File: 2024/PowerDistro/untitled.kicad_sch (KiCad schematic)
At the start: 40 parts

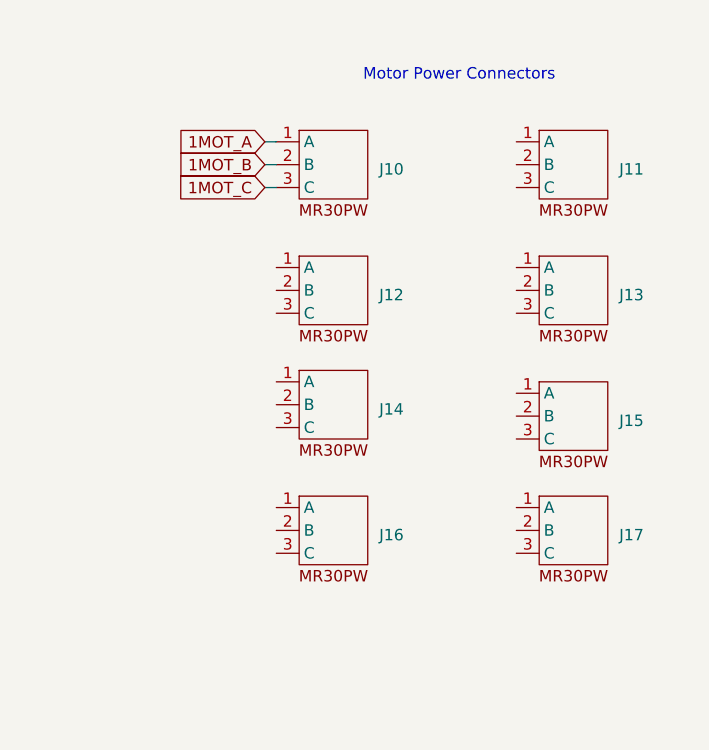
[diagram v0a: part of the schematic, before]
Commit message: changed motor controler numbers and hole numbers in PCB
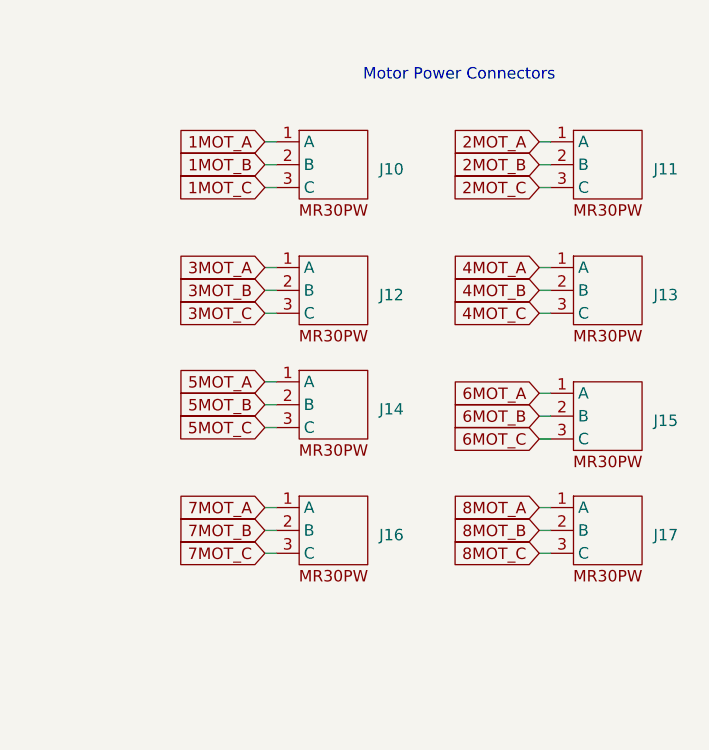
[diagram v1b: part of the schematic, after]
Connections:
- net 4MOT_A: now reaches J13.1 (A)
- net 4MOT_B: now reaches J13.2 (B)
- net 4MOT_C: now reaches J13.3 (C)
- net 7MOT_A: now reaches J16.1 (A)
- net 7MOT_B: now reaches J16.2 (B)
- net 7MOT_C: now reaches J16.3 (C)
- net 5MOT_A: now reaches J14.1 (A)
- net 5MOT_B: now reaches J14.2 (B)
- net 5MOT_C: now reaches J14.3 (C)
- net 6MOT_A: now reaches J15.1 (A)
- net 6MOT_B: now reaches J15.2 (B)
- net 6MOT_C: now reaches J15.3 (C)
- net 3MOT_A: now reaches J12.1 (A)
- net 3MOT_B: now reaches J12.2 (B)
- net 3MOT_C: now reaches J12.3 (C)
- net 2MOT_A: now reaches J11.1 (A)
- net 2MOT_B: now reaches J11.2 (B)
- net 2MOT_C: now reaches J11.3 (C)
- net 8MOT_A: now reaches J17.1 (A)
- net 8MOT_B: now reaches J17.2 (B)
- net 8MOT_C: now reaches J17.3 (C)
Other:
- moved on the sheet: J11, J13, J15, J17

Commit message: rearranged the power distro board
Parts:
- H1, H10, H11, H12, H13, H14, H15, H16, H17, H18, H19, H2, H20, H21, H22, H23, H24, H25, H26, H27, H28, H29, H3, H30, H31, H32, H4, H5, H6, H7, H8, H9: footprint (none) -> MountingHole:MountingHole_2.7mm_M2.5_ISO7380
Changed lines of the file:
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@@
 			)
 		)
-		(property "Footprint" ""
+		(property "Footprint" "MountingHole:MountingHole_2.7mm_M2.5_ISO7380"
 			(at 101.6 127 0)
 			(effects
@@
 			)
 		)
-		(property "Footprint" ""
+		(property "Footprint" "MountingHole:MountingHole_2.7mm_M2.5_ISO7380"
 			(at 101.6 81.28 0)
 			(effects
@@
 			)
 		)
-		(property "Footprint" ""
+		(property "Footprint" "MountingHole:MountingHole_2.7mm_M2.5_ISO7380"
 			(at 81.28 50.8 0)
 			(effects
@@
 			)
 		)
-		(property "Footprint" ""
+		(property "Footprint" "MountingHole:MountingHole_2.7mm_M2.5_ISO7380"
 			(at 101.6 119.38 0)
 			(effects
@@
 			)
 		)
-		(property "Footprint" ""
+		(property "Footprint" "MountingHole:MountingHole_2.7mm_M2.5_ISO7380"
 			(at 81.28 165.1 0)
 			(effects
@@
 			)
 		)
-		(property "Footprint" ""
+		(property "Footprint" "MountingHole:MountingHole_2.7mm_M2.5_ISO7380"
 			(at 81.28 127 0)
 			(effects
@@
 			)
 		)
-		(property "Footprint" ""
+		(property "Footprint" "MountingHole:MountingHole_2.7mm_M2.5_ISO7380"
 			(at 101.6 149.86 0)
 			(effects
@@
 			)
 		)
-		(property "Footprint" ""
+		(property "Footprint" "MountingHole:MountingHole_2.7mm_M2.5_ISO7380"
 			(at 101.6 88.9 0)
 			(effects
@@
 			)
 		)
-		(property "Footprint" ""
+		(property "Footprint" "MountingHole:MountingHole_2.7mm_M2.5_ISO7380"
 			(at 101.6 50.8 0)
 			(effects
@@
 			)
 		)
-		(property "Footprint" ""
+		(property "Footprint" "MountingHole:MountingHole_2.7mm_M2.5_ISO7380"
 			(at 101.6 66.04 0)
 			(effects
@@
 			)
 		)
-		(property "Footprint" ""
+		(property "Footprint" "MountingHole:MountingHole_2.7mm_M2.5_ISO7380"
 			(at 81.28 134.62 0)
 			(effects
@@
 			)
 		)
-		(property "Footprint" ""
+		(property "Footprint" "MountingHole:MountingHole_2.7mm_M2.5_ISO7380"
 			(at 101.6 142.24 0)
 			(effects
@@
 			)
 		)
-		(property "Footprint" ""
+		(property "Footprint" "MountingHole:MountingHole_2.7mm_M2.5_ISO7380"
 			(at 101.6 111.76 0)
 			(effects
@@
 			)
 		)
-		(property "Footprint" ""
+		(property "Footprint" "MountingHole:MountingHole_2.7mm_M2.5_ISO7380"
 			(at 101.6 165.1 0)
 			(effects
@@
 			)
 		)
-		(property "Footprint" ""
+		(property "Footprint" "MountingHole:MountingHole_2.7mm_M2.5_ISO7380"
 			(at 81.28 66.04 0)
 			(effects
@@
 			)
 		)
-		(property "Footprint" ""
+		(property "Footprint" "MountingHole:MountingHole_2.7mm_M2.5_ISO7380"
 			(at 101.6 73.66 0)
 			(effects
@@
 			)
 		)
-		(property "Footprint" ""
+		(property "Footprint" "MountingHole:MountingHole_2.7mm_M2.5_ISO7380"
 			(at 101.6 96.52 0)
 			(effects
@@
 			)
 		)
-		(property "Footprint" ""
+		(property "Footprint" "MountingHole:MountingHole_2.7mm_M2.5_ISO7380"
 			(at 81.28 81.28 0)
 			(effects
@@
 			)
 		)
-		(property "Footprint" ""
+		(property "Footprint" "MountingHole:MountingHole_2.7mm_M2.5_ISO7380"
 			(at 81.28 157.48 0)
 			(effects
@@
 			)
 		)
-		(property "Footprint" ""
+		(property "Footprint" "MountingHole:MountingHole_2.7mm_M2.5_ISO7380"
 			(at 101.6 104.14 0)
 			(effects
@@
 			)
 		)
-		(property "Footprint" ""
+		(property "Footprint" "MountingHole:MountingHole_2.7mm_M2.5_ISO7380"
 			(at 81.28 149.86 0)
 			(effects
@@
 			)
 		)
-		(property "Footprint" ""
+		(property "Footprint" "MountingHole:MountingHole_2.7mm_M2.5_ISO7380"
 			(at 81.28 104.14 0)
 			(effects
@@
 			)
 		)
-		(property "Footprint" ""
+		(property "Footprint" "MountingHole:MountingHole_2.7mm_M2.5_ISO7380"
 			(at 81.28 119.38 0)
 			(effects
@@
 			)
 		)
-		(property "Footprint" ""
+		(property "Footprint" "MountingHole:MountingHole_2.7mm_M2.5_ISO7380"
 			(at 81.28 73.66 0)
 			(effects
@@
 			)
 		)
-		(property "Footprint" ""
+		(property "Footprint" "MountingHole:MountingHole_2.7mm_M2.5_ISO7380"
 			(at 101.6 134.62 0)
 			(effects
@@
 			)
 		)
-		(property "Footprint" ""
+		(property "Footprint" "MountingHole:MountingHole_2.7mm_M2.5_ISO7380"
 			(at 81.28 58.42 0)
 			(effects
@@
 			)
 		)
-		(property "Footprint" ""
+		(property "Footprint" "MountingHole:MountingHole_2.7mm_M2.5_ISO7380"
 			(at 81.28 142.24 0)
 			(effects
@@
 			)
 		)
-		(property "Footprint" ""
+		(property "Footprint" "MountingHole:MountingHole_2.7mm_M2.5_ISO7380"
 			(at 81.28 88.9 0)
 			(effects
@@
 			)
 		)
-		(property "Footprint" ""
+		(property "Footprint" "MountingHole:MountingHole_2.7mm_M2.5_ISO7380"
 			(at 81.28 111.76 0)
 			(effects
@@
 			)
 		)
-		(property "Footprint" ""
+		(property "Footprint" "MountingHole:MountingHole_2.7mm_M2.5_ISO7380"
 			(at 101.6 58.42 0)
 			(effects
@@
 			)
 		)
-		(property "Footprint" ""
+		(property "Footprint" "MountingHole:MountingHole_2.7mm_M2.5_ISO7380"
 			(at 101.6 157.48 0)
 			(effects
@@
 			)
 		)
-		(property "Footprint" ""
+		(property "Footprint" "MountingHole:MountingHole_2.7mm_M2.5_ISO7380"
 			(at 81.28 96.52 0)
 			(effects

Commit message: Pushing so Power connector can be added
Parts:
- J10, J11, J12, J13, J14, J15, J16, J17: footprint PowerDistroFootprints:MR30PW-M -> PowerDistroFootprints:MR30PB
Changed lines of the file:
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@@
 			)
 		)
-		(property "Footprint" "PowerDistroFootprints:MR30PW-M"
+		(property "Footprint" "PowerDistroFootprints:MR30PB"
 			(at 204.47 69.85 0)
 			(effects
@@
 			)
 		)
-		(property "Footprint" "PowerDistroFootprints:MR30PW-M"
+		(property "Footprint" "PowerDistroFootprints:MR30PB"
 			(at 173.99 96.52 0)
 			(effects
@@
 			)
 		)
-		(property "Footprint" "PowerDistroFootprints:MR30PW-M"
+		(property "Footprint" "PowerDistroFootprints:MR30PB"
 			(at 173.99 55.88 0)
 			(effects
@@
 			)
 		)
-		(property "Footprint" "PowerDistroFootprints:MR30PW-M"
+		(property "Footprint" "PowerDistroFootprints:MR30PB"
 			(at 173.99 82.55 0)
 			(effects
@@
 			)
 		)
-		(property "Footprint" "PowerDistroFootprints:MR30PW-M"
+		(property "Footprint" "PowerDistroFootprints:MR30PB"
 			(at 204.47 83.82 0)
 			(effects
@@
 			)
 		)
-		(property "Footprint" "PowerDistroFootprints:MR30PW-M"
+		(property "Footprint" "PowerDistroFootprints:MR30PB"
 			(at 173.99 69.85 0)
 			(effects
@@
 			)
 		)
-		(property "Footprint" "PowerDistroFootprints:MR30PW-M"
+		(property "Footprint" "PowerDistroFootprints:MR30PB"
 			(at 204.47 55.88 0)
 			(effects
@@
 			)
 		)
-		(property "Footprint" "PowerDistroFootprints:MR30PW-M"
+		(property "Footprint" "PowerDistroFootprints:MR30PB"
 			(at 204.47 96.52 0)
 			(effects

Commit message: Added power layer to power distro motors
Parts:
- added H33, H34, H35, H36: MountingHole, MountingHole:MountingHole_4.3mm_M4_ISO7380, symbol Mechanical:MountingHole
- added J18: Conn_01x02_Pin, PowerDistroFootprints:XT90PB, symbol Connector:Conn_01x02_Pin
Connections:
- new net GND: J18.2 (Pin_2)
- new net PVDD: J18.1 (Pin_1)

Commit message: Changed Everything
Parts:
- removed H1, H10, H11, H12, H13, H14, H15, H16, H17, H18, H19, H2, H20, H21, H22, H23, H24, H25, H26, H27, H28, H29, H3, H30, H31, H32, H4, H5, H6, H7, H8, H9: MountingHole, MountingHole:MountingHole_2.7mm_M2.5_ISO7380, symbol Mechanical:MountingHole
- removed H33, H34, H35, H36: MountingHole, MountingHole:MountingHole_4.3mm_M4_ISO7380, symbol Mechanical:MountingHole
- removed J10, J11, J12, J13, J14, J15, J16, J17: ~, PowerDistroFootprints:MR30PB, symbol PowerDistro:MR30PW-M
- added J1, J2, J3, J4, J5, J6: Screw_Terminal_01x03, PowerDistroFootprints:691311500103, symbol Connector:Screw_Terminal_01x03
- added J10, J11, J12: Screw_Terminal_01x02, PowerDistroFootprints:691311500102, symbol Connector:Screw_Terminal_01x02
- added J7, J8: Conn_01x02_Pin, Connector_PinHeader_2.54mm:PinHeader_1x02_P2.54mm_Vertical, symbol Connector:Conn_01x02_Pin
- added U2, U3, U4, U5, U6, U7: ~, PowerDistroFootprints:BlueRoboticsESC, symbol PowerDistro:BlueRoboticsESC
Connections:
- net GND: now also J10.2 (Pin_2), J11.2 (Pin_2), J12.2 (Pin_2), J7.2 (Pin_2), J8.2 (Pin_2), U2.5 (GND), U2.7 (SGND), U3.5 (GND), U3.7 (SGND), U4.5 (GND), U4.7 (SGND), U5.5 (GND), U5.7 (SGND), U6.5 (GND), U6.7 (SGND), U7.5 (GND), U7.7 (SGND)
- net PVDD: now also J10.1 (Pin_1), J11.1 (Pin_1), J12.1 (Pin_1), U2.4 (VDD), U3.4 (VDD), U4.4 (VDD), U5.4 (VDD), U6.4 (VDD), U7.4 (VDD)
- new net: J3.1 (Pin_1), U4.1 (A)
- new net: J3.2 (Pin_2), U4.2 (B)
- new net: J3.3 (Pin_3), U4.3 (C)
- new net: J2.1 (Pin_1), U3.1 (A)
- new net: J2.2 (Pin_2), U3.2 (B)
- new net: J2.3 (Pin_3), U3.3 (C)
- new net: J6.1 (Pin_1), U7.1 (A)
- new net: J6.2 (Pin_2), U7.2 (B)
- new net: J6.3 (Pin_3), U7.3 (C)
- new net: J1.1 (Pin_1), U2.1 (A)
- new net: J1.2 (Pin_2), U2.2 (B)
- new net: J1.3 (Pin_3), U2.3 (C)
- new net: J5.1 (Pin_1), U6.1 (A)
- new net: J5.2 (Pin_2), U6.2 (B)
- new net: J5.3 (Pin_3), U6.3 (C)
- new net: J4.1 (Pin_1), U5.1 (A)
- new net: J4.2 (Pin_2), U5.2 (B)
- new net: J4.3 (Pin_3), U5.3 (C)
- new net PWM1: U5.6 (PWM)
- new net PWM2: U6.6 (PWM)
- new net PWM3: U7.6 (PWM)
- new net PWM4: U3.6 (PWM)
- new net PWM5: U2.6 (PWM)
- new net PWM6: U4.6 (PWM)
- new net PWM7: J7.1 (Pin_1)
- new net PWM8: J8.1 (Pin_1)
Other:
- note added: "Connections For Extra Motors"
- note added: "Main Power"
- note added: "Motor Drivers"
- note removed: "Motor Power Connectors"
- note removed: "Mouning Holes"
- moved on the sheet: J18

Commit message: Release
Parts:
- added H1, H2, H3, H4: MountingHole, MountingHole:MountingHole_5.3mm_M5, symbol Mechanical:MountingHole
- J10, J11, J12: footprint PowerDistroFootprints:691311500102 -> PowerDistroFootprints:691321100002
- J18: value Conn_01x02_Pin -> XT90
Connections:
- net GND: now also J18.1 (Pin_1); no longer J18.2 (Pin_2)
- net PVDD: now also J18.2 (Pin_2); no longer J18.1 (Pin_1)

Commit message: Update to KiCad 10.0
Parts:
- U2, U3, U4, U5, U6, U7: value ~ -> (none)
